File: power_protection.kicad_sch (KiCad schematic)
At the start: 0 parts

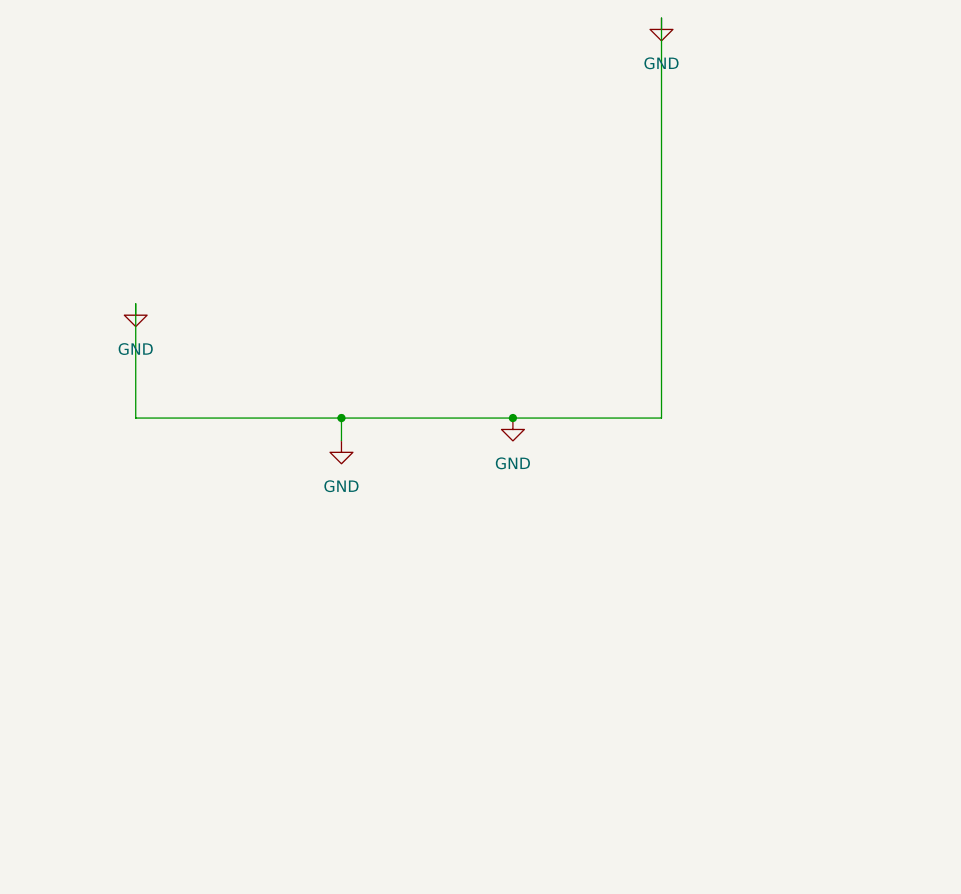
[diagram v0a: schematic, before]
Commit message: Updated Power Protection
Added:
- Solder Jumper
- Two Input Voltages 3.3 and 5.0
- Voltage Regulators
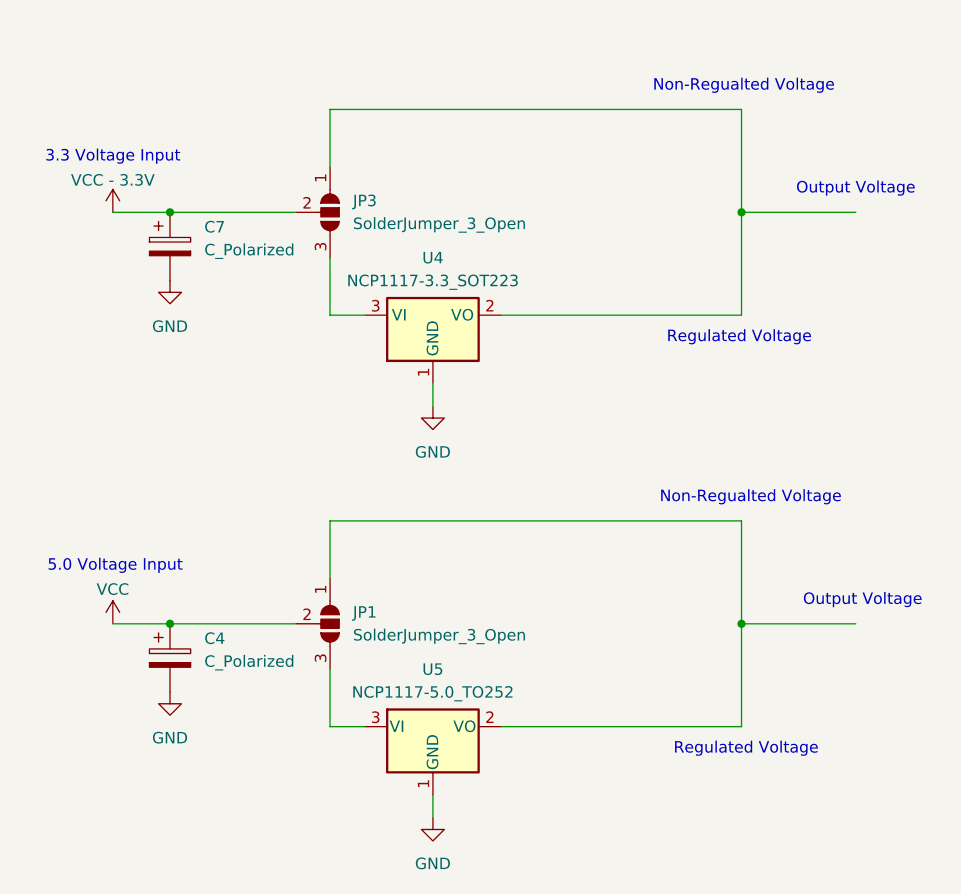
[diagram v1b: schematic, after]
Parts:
- added C4, C7: C_Polarized, symbol Device:C_Polarized
- added JP1, JP3: SolderJumper_3_Open, symbol Jumper:SolderJumper_3_Open
- added U4: NCP1117-3.3_SOT223, Package_TO_SOT_SMD:SOT-223-3_TabPin2, symbol Regulator_Linear:NCP1117-3.3_SOT223
- added U5: NCP1117-5.0_TO252, Package_TO_SOT_SMD:TO-252-2, symbol Regulator_Linear:NCP1117-5.0_TO252
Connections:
- net GND: now also C4.2, C7.2, U4.1 (GND), U5.1 (GND)
- new net: JP3.1 (A), U4.2 (VO)
- new net: JP3.3 (B), U4.3 (VI)
- new net: JP1.1 (A), U5.2 (VO)
- new net: JP1.3 (B), U5.3 (VI)
- new net VCC: C4.1, JP1.2 (C)
- new net VCC - 3.3V: C7.1, JP3.2 (C)
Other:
- note added: "3.3 Voltage Input"
- note added: "5.0 Voltage Input"
- note added: "Non-Regualted Voltage"
- note added: "Output Voltage"
- note added: "Regulated Voltage"
